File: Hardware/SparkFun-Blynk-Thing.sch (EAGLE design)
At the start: 100 parts, among them J1 M01ALLIGATOR_HALF, J10 M01ALLIGATOR_HALF, J11 M01ALLIGATOR_HALF, J12 M01ALLIGATOR_HALF, J2 M01ALLIGATOR_HALF, J3 M01ALLIGATOR_HALF, J4 M01ALLIGATOR_HALF, J5 M01ALLIGATOR_HALF, J6 M01ALLIGATOR_HALF, J7 M01ALLIGATOR_HALF, J8 M01ALLIGATOR_HALF, J9 M01ALLIGATOR_HALF, Q1 MMBT2222A, Q2 MMBT2222A, Q3 2.5A/30V, U2 ESP8266, U3 W25Q32FVSS, U4 FT231XS-U, U5 SI7021, U6 MCP73831, U7 AP2112K-3.3V, U8 OPAMP-DUALU, Y1 26MHz

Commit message: Schematic cleanup
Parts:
- removed C19: 2.2uF, SparkFun-Capacitors:2.2UF-10V-20%(0603)
- removed D7: RED, SparkFun-LED:LED-RED0603
- removed J1, J10, J12, J5, J7, J8, J9: M01ALLIGATOR_HALF, blynk-thing-temp:M01ALLIGATOR_HALF
- removed R22: 2.0k, SparkFun-Resistors:2.0KOHM1/10W5%(0603)
- removed R25: 22K, SparkFun-Resistors:22KOHM1/10W1%(0603)
- removed R26: 10K, SparkFun-Resistors:10KOHM-1/10W-1%(0603)0603
- removed U7: AP2112K-3.3V, SparkFun-PowerIC:V_REG_LDOSMD
- added C5: 0.1uF, SparkFun-Capacitors:0.1UF-25V(+80/-20%)(0603)
- added D2: BAT20J, SparkFun-DiscreteSemi:DIODE-SCHOTTKY-BAT20J
- added JP19, JP21, JP23, JP25, JP27, JP28: (no value), SparkFun-Connectors:M01PTH_NO_SILK_YES_STOP
- added JP29: (no value), SparkFun-Connectors:M04JST-PTH-VERT
- added R11: 330, SparkFun-Resistors:330OHM1/10W1%(0603)
- added R13: 27, SparkFun-Resistors:27OHM1/10W1%(0603)0603-RES
- added R15: 4.7K, SparkFun-Resistors:4.7KOHM-1/10W-1%(0603)
- added U1: MCP73831, SparkFun-PowerIC:MCP73831
- C10: value 0.1uF -> 2.2uF; device SparkFun-Capacitors:0.1UF-25V(+80/-20%)(0603) -> SparkFun-Capacitors:2.2UF-10V-20%(0603)
- C11, C9: value 47pF -> 0.1uF; device SparkFun-Capacitors:47PF-50V-5%(0603) -> SparkFun-Capacitors:0.1UF-25V(+80/-20%)(0603)
- C12: value 0.1uF -> 47pF; device SparkFun-Capacitors:0.1UF-25V(+80/-20%)(0603) -> SparkFun-Capacitors:47PF-50V-5%(0603)
- C13: value 4.7uF -> 47pF; device SparkFun-Capacitors:4.7UF-6.3V-10%(0603)0603 -> SparkFun-Capacitors:47PF-50V-5%(0603)
- C15: value 0.1uF -> 4.7uF; device SparkFun-Capacitors:0.1UF-25V(+80/-20%)(0603) -> SparkFun-Capacitors:4.7UF-6.3V-10%(0603)0603
- C18: value 1.0uF -> 0.1uF; device SparkFun-Capacitors:1.0UF-25V-+80/-20(0805)" -> SparkFun-Capacitors:0.1UF-25V(+80/-20%)(0603)
- C7: value 5.6pF -> 1.0uF; device SparkFun-Capacitors:CAP0603-CAP -> SparkFun-Capacitors:1.0UF-25V-+80/-20(0805)"; PROD_ID CAP-12456 -> (none)
- C8: value 0.1uF -> 5.6pF; device SparkFun-Capacitors:0.1UF-25V(+80/-20%)(0603) -> SparkFun-Capacitors:CAP0603-CAP; PROD_ID (none) -> CAP-12456
- D3: value (none) -> BLUE; device SparkFun-LED:WS2812B -> SparkFun-LED:LED-BLUE0603
- D4: value BLUE -> (none); device SparkFun-LED:LED-BLUE0603 -> SparkFun-LED:WS2812B
- D5: value BAT20J -> RED; device SparkFun-DiscreteSemi:DIODE-SCHOTTKY-BAT20J -> SparkFun-LED:LED-RED0603
- JP1: value (none) -> LiPo; device SparkFun-Connectors:USB_MICROB_PLUGCONN-11752 -> SparkFun-Connectors:M02JST-PTH-2
- JP10, JP12, JP16, JP4, JP6, JP8: value (none) -> M01ALLIGATOR_HALF; device SparkFun-Connectors:M01PTH_NO_SILK_YES_STOP -> blynk-thing-temp:M01ALLIGATOR_HALF
- JP13: value LiPo -> (none); device SparkFun-Connectors:M02JST-PTH-2 -> SparkFun-Connectors:M01PTH_NO_SILK_YES_STOP
- JP14: device SparkFun-Connectors:M01PTH_NO_SILK_YES_STOP -> SparkFun-Connectors:M03JST-PTH-VERT
- JP15: device SparkFun-Connectors:M01PTH_NO_SILK_YES_STOP -> SparkFun-Connectors:USB_MICROB_PLUGCONN-11752
- JP2: value (none) -> M01ALLIGATOR_HALF; device SparkFun-Connectors:M04JST-PTH-VERT -> blynk-thing-temp:M01ALLIGATOR_HALF
- JP3: device SparkFun-Connectors:M03JST-PTH-VERT -> SparkFun-Connectors:M01PTH_NO_SILK_YES_STOP
- Q1: value MMBT2222A -> 2.5A/30V; device SparkFun-DiscreteSemi:TRANSISTOR_NPNMMBT2222A -> SparkFun-DiscreteSemi:MOSFET-PCHANNELDMG2307L
- Q3: value 2.5A/30V -> MMBT2222A; device SparkFun-DiscreteSemi:MOSFET-PCHANNELDMG2307L -> SparkFun-DiscreteSemi:TRANSISTOR_NPNMMBT2222A
- R14: value 10K -> 27; device SparkFun-Resistors:10KOHM1/10W1%(0603)0603 -> SparkFun-Resistors:27OHM1/10W1%(0603)0603-RES
- R16: value 330 -> 4.7K; device SparkFun-Resistors:330OHM1/10W1%(0603) -> SparkFun-Resistors:4.7KOHM-1/10W-1%(0603)
- R18: value 4.7K -> 10K; device SparkFun-Resistors:4.7KOHM-1/10W-1%(0603) -> SparkFun-Resistors:10KOHM1/10W1%(0603)0603
- R2: value 10K -> 1K; device SparkFun-Resistors:10KOHM1/10W1%(0603)0603 -> SparkFun-Resistors:1KOHM-1/10W-1%(0603)
- R20: value 1K -> 10K; device SparkFun-Resistors:1KOHM-1/10W-1%(0603) -> SparkFun-Resistors:10KOHM1/10W1%(0603)0603
- R3: value DNP -> 22K; device SparkFun-Passives:RESISTORPTH-1/6W -> SparkFun-Resistors:22KOHM1/10W1%(0603)
- R4: value 200 -> 10K; device SparkFun-Resistors:200OHM1/10W1%(0603) -> SparkFun-Resistors:10KOHM-1/10W-1%(0603)0603
- R5: value 10K -> DNP; device SparkFun-Resistors:10KOHM1/10W1%(0603)0603 -> SparkFun-Passives:RESISTORPTH-1/6W
- R6: value 4.7K -> 2.0k; device SparkFun-Resistors:4.7KOHM-1/10W-1%(0603) -> SparkFun-Resistors:2.0KOHM1/10W5%(0603)
- R7, R8: value 27 -> 10K; device SparkFun-Resistors:27OHM1/10W1%(0603)0603-RES -> SparkFun-Resistors:10KOHM1/10W1%(0603)0603
- R9: value 10K -> 200; device SparkFun-Resistors:10KOHM1/10W1%(0603)0603 -> SparkFun-Resistors:200OHM1/10W1%(0603)
- SJ1: value JUMPER-PAD-3-NC_BY_PASTE -> JUMPER-PAD-2-NC_BY_TRACE; device SparkFun-Passives:JUMPER-PAD-3-NC_BY_PASTE -> SparkFun-Passives:JUMPER-PAD-2-NC_BY_TRACE
- SJ2: value JUMPER-PAD-2-NC_BY_TRACE -> PWRLED
- SJ3: value PWRLED -> JUMPER-PAD-3-NC_BY_PASTE; device SparkFun-Passives:JUMPER-PAD-2-NC_BY_TRACE -> SparkFun-Passives:JUMPER-PAD-3-NC_BY_PASTE
- U3: value W25Q32FVSS -> AP2112K-3.3V; device blynk-thing-temp:W25Q32FVSS -> SparkFun-PowerIC:V_REG_LDOSMD; PROD_ID (none) -> VREG-12457
- U5: value SI7021 -> W25Q32FVSS; device SparkFun-Sensors:SI7021 -> blynk-thing-temp:W25Q32FVSS
- U6: value MCP73831 -> SI7021; device SparkFun-PowerIC:MCP73831 -> SparkFun-Sensors:SI7021
- renumbered C20 to C6, D6 to D1, J11 to JP26, J2 to JP18, J3 to JP22, J4 to JP24, J6 to JP20, R21 to R12, U8 to IC1
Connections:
- net 0/BUTTON: now also JP27.1, Q3.C, R19.1; no longer JP16.1, Q2.C, R14.1
- net 14/SCL: now also JP29.4, R16.1, U6.SCK; no longer JP2.4, R18.1, U5.SCK
- net 2/SDA: now also JP29.3, R15.1, U6.DATA; no longer JP2.3, R6.1, U5.DATA
- net 3.3V_F: now also C16.1; no longer C14.1
- net 4/WS2812: now also D4.DIN; no longer D3.DIN
- net ADC-IN: now also JP21.1; no longer JP6.1
- net CHIP_EN: now also R8.1; no longer R2.1
- net D+: now also C13.1, JP15.D+, R14.1; no longer C11.1, JP1.D+, R8.1
- net D-: now also C12.1, JP15.D-, R13.1; no longer C9.1, JP1.D-, R7.1
- net DTR: now also Q3.E, R17.1; no longer Q2.E, R9.1
- net GND: now also C5.2, C7.2, D4.VSS, JP1.1, JP14.2, JP15.GND, JP29.1, JP6.1, JP7.1, R11.2, R20.1, R4.1, R5.1, R6.1, R7.1, SJ2.1, U1.VSS, U6.GND; no longer C19.2, C8.2, D3.VSS, J8.1, JP1.GND, JP13.1, JP2.1, JP3.2, JP8.1, R16.2, R17.1, R19.1, R22.1, R26.1, R3.1, SJ3.1, U6.VSS, U7.GND
- net GPIO12: now also JP16.1, JP17.1; no longer J1.1, JP12.1
- net GPIO13: now also JP19.1; no longer JP11.1
- net GPIO15: now also JP23.1, R20.2; no longer JP10.1, R17.2
- net GPIO16: now also JP25.1; no longer JP9.1
- net GPIO5: now also D3.A, JP12.1, JP13.1; no longer D4.A, J5.1, JP5.1
- net LNA: now also C8.1; no longer C7.1
- net N$10: now also D5.A; no longer D7.A
- net N$11: now also R15.2, SJ3.3; no longer R6.2, SJ1.3
- net N$12: now also Q3.B, R18.2; no longer Q2.B, R10.2
- net N$13: now also R16.2, SJ3.1; no longer R18.2, SJ1.1
- net N$14: now also R5.2, SJ1.2, U1.PROG; no longer R3.2, SJ2.2, U6.PROG
- net N$15: now also R3.2; no longer R25.2
- net N$16: now also R6.2, SJ1.1; no longer R22.2, SJ2.1
- net N$17: now also R2.2; no longer R20.2
- net N$18: now also R3.1, R4.2; no longer R25.1, R26.2
- net N$4: now also R13.2; no longer R7.2
- net N$5: now also D5.C, SJ2.2; no longer D7.C, SJ3.2
- net N$6: now also Q2.B, R17.2; no longer Q1.B, R9.2
- net N$7: now also R14.2; no longer R8.2
- net N$8: now also D3.C, R11.1; no longer D4.C, R16.1
- net N$9: now also R2.1, U1.STAT; no longer R20.1, U6.STAT
- net RESET: now also JP28.1, Q2.C, R10.1; no longer JP4.1, Q1.C, R5.1
- net RTS: now also Q2.E, R18.1; no longer Q1.E, R10.1
- net SD_!HD!: now also U5.!HOLD!(D3); no longer U3.!HOLD!(D3)
- net SD_!WP!: now also U5.!WP!(D2); no longer U3.!WP!(D2)
- net SD_CLK: now also R9.1, U5.SCK; no longer R4.1, U3.SCK
- net SD_CLK0: now also R9.2; no longer R4.2
- net SD_CS0: now also U5.!CS!; no longer U3.!CS!
- net SD_SI: now also U5.SI(D0); no longer U3.SI(D0)
- net SD_SO: now also U5.SO(D1); no longer U3.SO(D1)
- net SHIELD: now also JP15.SHIELD; no longer JP1.SHIELD
- net TRACE_ANT: now also C8.2; no longer C7.2
- net U0RXI: now also JP8.1, JP9.1; no longer J10.1, JP15.1
- net U0TXO: now also JP10.1, JP11.1; no longer J9.1, JP14.1
- net VBAT: now also JP1.2, Q1.D, U1.VBAT; no longer JP13.2, Q3.D, U6.VBAT
- net VCC: now also C18.1, C5.1, C9.1, D4.VDD, JP14.1, JP29.2, JP4.1, JP5.1, R10.2, R19.2, R8.2, SJ3.2, U3.OUT, U5.VCC, U6.VDD; no longer C15.1, C16.1, C19.1, D3.VDD, J7.1, JP2.2, JP3.1, JP7.1, R14.2, R2.2, R5.2, SJ1.2, U3.VCC, U5.VDD, U7.OUT
- net VIN: now also C7.1, D2.C, JP2.1, JP3.1, Q1.S, U3.EN, U3.IN; no longer C18.1, D5.C, J12.1, JP17.1, Q3.S, U7.EN, U7.IN
- net VUSB: now also C11.1, JP15.VCC; no longer C8.1, JP1.VCC
- net V_USB: now also C14.1, C15.1, D2.A, Q1.G, R7.2, U1.VIN; no longer C12.1, C13.1, D5.A, Q3.G, R19.2, U6.VIN
- net WS2812-DOUT: now also D4.DOUT, JP14.3; no longer D3.DOUT, JP3.3
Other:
- note added: "SJ1 can be cut to modify the charge- current programming resistor."
- note added: "SJ2 can be cut to disable the power LED. (Saving lots of power.)"
- note added: "SJ3 can be cleared to remove the pull-up resistors from SDA and SCL. (NOTE: GPIO2 _must_ be pulled high to run.)"
- note added: "Si7021 I2C Address: 0x40"
- note removed: "SJ1 can be cut to disable the power LED. (Saving lots of power.)"
- moved on the sheet: C10, C11, C12, C13, C14, C15, C16, C17, C18, C7, C8, C9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

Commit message: Board cleanup
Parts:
- U2: device esp8266-development-board:ESP8266 -> SparkFun-RF:ESP8266
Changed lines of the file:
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@@
 <grid distance="0.1" unitdist="inch" unit="inch" style="lines" multiple="1" display="no" altdistance="0.01" altunitdist="inch" altunit="inch"/>
 <layers>
-<layer number="1" name="Top" color="4" fill="1" visible="no" active="no"/>
-<layer number="2" name="Route2" color="1" fill="3" visible="no" active="no"/>
-<layer number="3" name="Route3" color="4" fill="3" visible="no" active="no"/>
-<layer number="4" name="Route4" color="1" fill="4" visible="no" active="no"/>
-<layer number="5" name="Route5" color="4" fill="4" visible="no" active="no"/>
-<layer number="6" name="Route6" color="1" fill="8" visible="no" active="no"/>
-<layer number="7" name="Route7" color="4" fill="8" visible="no" active="no"/>
-<layer number="8" name="Route8" color="1" fill="2" visible="no" active="no"/>
-<layer number="9" name="Route9" color="4" fill="2" visible="no" active="no"/>
-<layer number="10" name="Route10" color="1" fill="7" visible="no" active="no"/>
-<layer number="11" name="Route11" color="4" fill="7" visible="no" active="no"/>
-<layer number="12" name="Route12" color="1" fill="5" visible="no" active="no"/>
-<layer number="13" name="Route13" color="4" fill="5" visible="no" active="no"/>
-<layer number="14" name="Route14" color="1" fill="6" visible="no" active="no"/>
-<layer number="15" name="Route15" color="4" fill="6" visible="no" active="no"/>
-<layer number="16" name="Bottom" color="1" fill="1" visible="no" active="no"/>
-<layer number="17" name="Pads" color="2" fill="1" visible="no" active="no"/>
-<layer number="18" name="Vias" color="2" fill="1" visible="no" active="no"/>
-<layer number="19" name="Unrouted" color="6" fill="1" visible="no" active="no"/>
-<layer number="20" name="Dimension" color="15" fill="1" visible="no" active="no"/>
-<layer number="21" name="tPlace" color="16" fill="1" visible="no" active="no"/>
-<layer number="22" name="bPlace" color="14" fill="1" visible="no" active="no"/>
-<layer number="23" name="tOrigins" color="15" fill="1" visible="no" active="no"/>
-<layer number="24" name="bOrigins" color="15" fill="1" visible="no" active="no"/>
-<layer number="25" name="tNames" color="7" fill="1" visible="no" active="no"/>
-<layer number="26" name="bNames" color="7" fill="1" visible="no" active="no"/>
-<layer number="27" name="tValues" color="7" fill="1" visible="no" active="no"/>
-<layer number="28" name="bValues" color="7" fill="1" visible="no" active="no"/>
+<layer number="1" name="Top" color="4" fill="1" visible="yes" active="no"/>
+<layer number="2" name="Route2" color="1" fill="3" visible="yes" active="no"/>
+<layer number="3" name="Route3" color="4" fill="3" visible="yes" active="no"/>
+<layer number="4" name="Route4" color="1" fill="4" visible="yes" active="no"/>
+<layer number="5" name="Route5" color="4" fill="4" visible="yes" active="no"/>
+<layer number="6" name="Route6" color="1" fill="8" visible="yes" active="no"/>
+<layer number="7" name="Route7" color="4" fill="8" visible="yes" active="no"/>
+<layer number="8" name="Route8" color="1" fill="2" visible="yes" active="no"/>
+<layer number="9" name="Route9" color="4" fill="2" visible="yes" active="no"/>
+<layer number="10" name="Route10" color="1" fill="7" visible="yes" active="no"/>
+<layer number="11" name="Route11" color="4" fill="7" visible="yes" active="no"/>
+<layer number="12" name="Route12" color="1" fill="5" visible="yes" active="no"/>
+<layer number="13" name="Route13" color="4" fill="5" visible="yes" active="no"/>
+<layer number="14" name="Route14" color="1" fill="6" visible="yes" active="no"/>
+<layer number="15" name="Route15" color="4" fill="6" visible="yes" active="no"/>
+<layer number="16" name="Bottom" color="1" fill="1" visible="yes" active="no"/>
+<layer number="17" name="Pads" color="2" fill="1" visible="yes" active="no"/>
+<layer number="18" name="Vias" color="2" fill="1" visible="yes" active="no"/>
+<layer number="19" name="Unrouted" color="6" fill="1" visible="yes" active="no"/>
+<layer number="20" name="Dimension" color="15" fill="1" visible="yes" active="no"/>
+<layer number="21" name="tPlace" color="16" fill="1" visible="yes" active="no"/>
+<layer number="22" name="bPlace" color="14" fill="1" visible="yes" active="no"/>
+<layer number="23" name="tOrigins" color="15" fill="1" visible="yes" active="no"/>
+<layer number="24" name="bOrigins" color="15" fill="1" visible="yes" active="no"/>
+<layer number="25" name="tNames" color="7" fill="1" visible="yes" active="no"/>
+<layer number="26" name="bNames" color="7" fill="1" visible="yes" active="no"/>
+<layer number="27" name="tValues" color="7" fill="1" visible="yes" active="no"/>
+<layer number="28" name="bValues" color="7" fill="1" visible="yes" active="no"/>
 <layer number="29" name="tStop" color="7" fill="3" visible="no" active="no"/>
 <layer number="30" name="bStop" color="7" fill="6" visible="no" active="no"/>
@@
 <layer number="35" name="tGlue" color="7" fill="4" visible="no" active="no"/>
 <layer number="36" name="bGlue" color="7" fill="5" visible="no" active="no"/>
-<layer number="37" name="tTest" color="7" fill="1" visible="no" active="no"/>
-<layer number="38" name="bTest" color="7" fill="1" visible="no" active="no"/>
+<layer number="37" name="tTest" color="7" fill="1" visible="yes" active="no"/>
+<layer number="38" name="bTest" color="7" fill="1" visible="yes" active="no"/>
 <layer number="39" name="tKeepout" color="4" fill="11" visible="no" active="no"/>
 <layer number="40" name="bKeepout" color="1" fill="11" visible="no" active="no"/>
@@
 <layer number="44" name="Drills" color="7" fill="1" visible="no" active="no"/>
 <layer number="45" name="Holes" color="7" fill="1" visible="no" active="no"/>
-<layer number="46" name="Milling" color="3" fill="1" visible="no" active="no"/>
-<layer number="47" name="Measures" color="7" fill="1" visible="no" active="no"/>
-<layer number="48" name="Document" color="7" fill="1" visible="no" active="no"/>
-<layer number="49" name="Reference" color="7" fill="1" visible="no" active="no"/>
-<layer number="50" name="dxf" color="7" fill="1" visible="no" active="no"/>
-<layer number="51" name="tDocu" color="6" fill="1" visible="no" active="no"/>
-<layer number="52" name="bDocu" color="7" fill="1" visible="no" active="no"/>
-<layer number="53" name="tGND_GNDA" color="7" fill="9" visible="no" active="no"/>
-<layer number="54" name="bGND_GNDA" color="1" fill="9" visible="no" active="no"/>
-<layer number="56" name="wert" color="7" fill="1" visible="no" active="no"/>
-<layer number="57" name="tCAD" color="7" fill="1" visible="no" active="no"/>
-<layer number="59" name="tCarbon" color="7" fill="1" visible="no" active="no"/>
-<layer number="60" name="bCarbon" color="7" fill="1" visible="no" active="no"/>
+<layer number="46" name="Milling" color="3" fill="1" visible="yes" active="no"/>
+<layer number="47" name="Measures" color="7" fill="1" visible="yes" active="no"/>
+<layer number="48" name="Document" color="7" fill="1" visible="yes" active="no"/>
+<layer number="49" name="Reference" color="7" fill="1" visible="yes" active="no"/>
+<layer number="50" name="dxf" color="7" fill="1" visible="yes" active="no"/>
+<layer number="51" name="tDocu" color="6" fill="1" visible="yes" active="no"/>
+<layer number="52" name="bDocu" color="7" fill="1" visible="yes" active="no"/>
+<layer number="53" name="tGND_GNDA" color="7" fill="9" visible="yes" active="no"/>
+<layer number="54" name="bGND_GNDA" color="1" fill="9" visible="yes" active="no"/>
+<layer number="56" name="wert" color="7" fill="1" visible="yes" active="no"/>
+<layer number="57" name="tCAD" color="7" fill="1" visible="yes" active="no"/>
+<layer number="59" name="tCarbon" color="7" fill="1" visible="yes" active="no"/>
+<layer number="60" name="bCarbon" color="7" fill="1" visible="yes" active="no"/>
 <layer number="90" name="Modules" color="5" fill="1" visible="yes" active="yes"/>
 <layer number="91" name="Nets" color="2" fill="1" visible="yes" active="yes"/>
@@
 </classes>
 <parts>
-<part name="U2" library="esp8266-development-board" deviceset="ESP8266" device="">
+<part name="U2" library="SparkFun-RF" deviceset="ESP8266" device="">
 <attribute name="PROD_ID" value="IC-12452"/>
 </part>

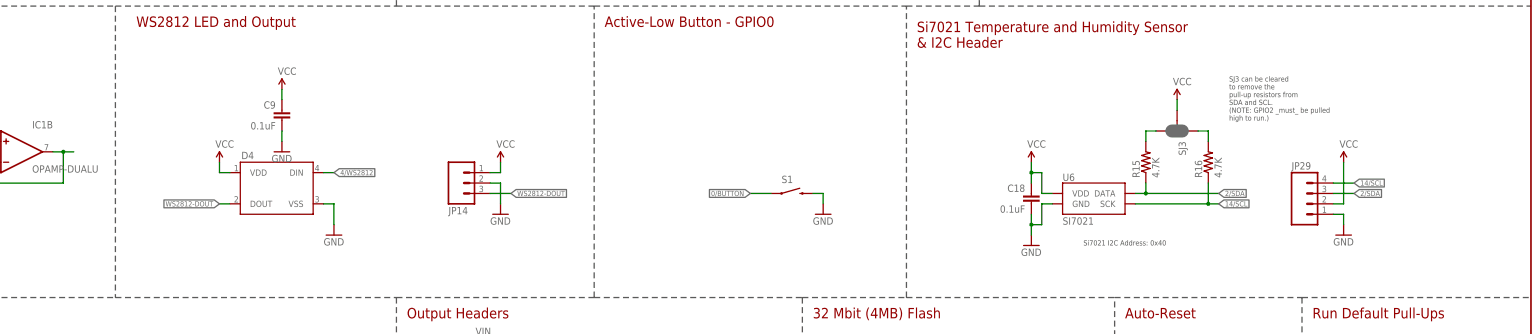
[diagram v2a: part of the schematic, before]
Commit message: Re-configuring the I2C connector.
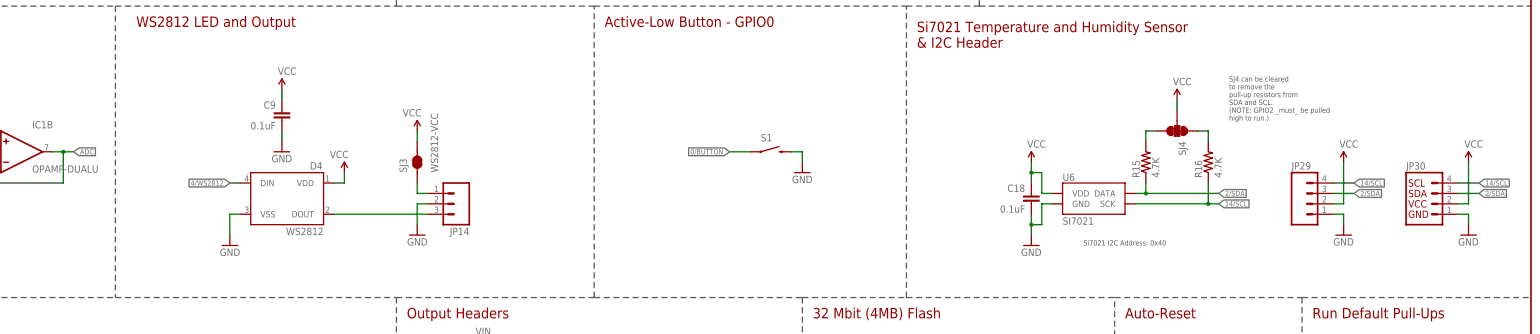
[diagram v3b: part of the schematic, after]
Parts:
- added JP30: (no value), SparkFun-Connectors:I2C_STANDARD_NO_SILK
- added SJ4: (no value), SparkFun-Passives:JUMPER-PAD-3-NC_BY_TRACE
- D4: value (none) -> WS2812
- JP29: device SparkFun-Connectors:M04JST-PTH-VERT -> SparkFun-Connectors:M04JST
- SJ3: value JUMPER-PAD-3-NC_BY_PASTE -> WS2812-VCC; device SparkFun-Passives:JUMPER-PAD-3-NC_BY_PASTE -> SparkFun-Passives:JUMPER-PAD-2-NC_BY_TRACE
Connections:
- new net N$19: JP14.1, SJ3.1
- net 14/SCL: now also JP30.4
- net 2/SDA: now also JP30.3
- net GND: now also JP30.1
- net N$11: now also SJ4.3; no longer SJ3.3
- net N$13: now also SJ4.1; no longer SJ3.1
- net VCC: now also JP30.2, SJ4.2; no longer JP14.1
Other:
- note added: "SJ4 can be cleared to remove the pull-up resistors from SDA and SCL. (NOTE: GPIO2 _must_ be pulled high to run.)"
- note removed: "SJ3 can be cleared to remove the pull-up resistors from SDA and SCL. (NOTE: GPIO2 _must_ be pulled high to run.)"
- moved on the sheet: D4, JP14, S1

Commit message: Schematic cleanup, adding decoupling cap to batt charger
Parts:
- added C19: 4.7uF, SparkFun-Capacitors:4.7UF-6.3V-10%(0603)0603
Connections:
- net VBAT renamed V_BATT
- removed net RXLED: U4.CBUS1
- removed net TXLED: U4.CBUS2
- net GND: now also C19.2
- net V_USB: now also C19.1
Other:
- note added: "Charge current: I_CHG = 1000 / R_PROG R_PROG=2k : I_CHG=500mA"
- note added: "Lithium-Polymer Battery Charger (1-cell)"
- note added: "Power LED"
- note added: "SJ3 can be cut to avoid powering a WS2812 string with VCC. In case a higher-power source is required."
- note removed: "Charge current: 500mA"
- moved on the sheet: C10, C11, C12, C13, C14, C15, C16, C6, C7, C9, D1, D2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

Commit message: Schematic clean-up and some PROD_ID's
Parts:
- IC1: value OPAMP-DUALU -> LMV358; PROD_ID (none) -> IC-09657
- JP14: PROD_ID (none) -> TBD
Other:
- note added: "600mA out 6V max in"
- note added: "V_ADC = V_ADC-IN * 10 / 32 V_ADC-IN = V_ADC * 32/10 e.g.: 3.3V in : 1.03 out"
- note added: "V_BATT should be a single- cell LiPo battery."
- note removed: "VBAT should be a single- cell LiPo battery."
- moved on the sheet: C1, C2, C3, C4, C8, D3, E1, L1, L2, R1, R10, R11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
